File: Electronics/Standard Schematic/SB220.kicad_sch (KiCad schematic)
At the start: 134 parts, among them J1 Ant Relay, J2 ALC, J3 RF Input, J4 RF Output, J5 Screw_Terminal_01x04, J6 Screw_Terminal_01x04, J7 Screw_Terminal_01x04, K1 SB-220 Relay, M1 Fan Motor, P1 120/240 VAC 60Hz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

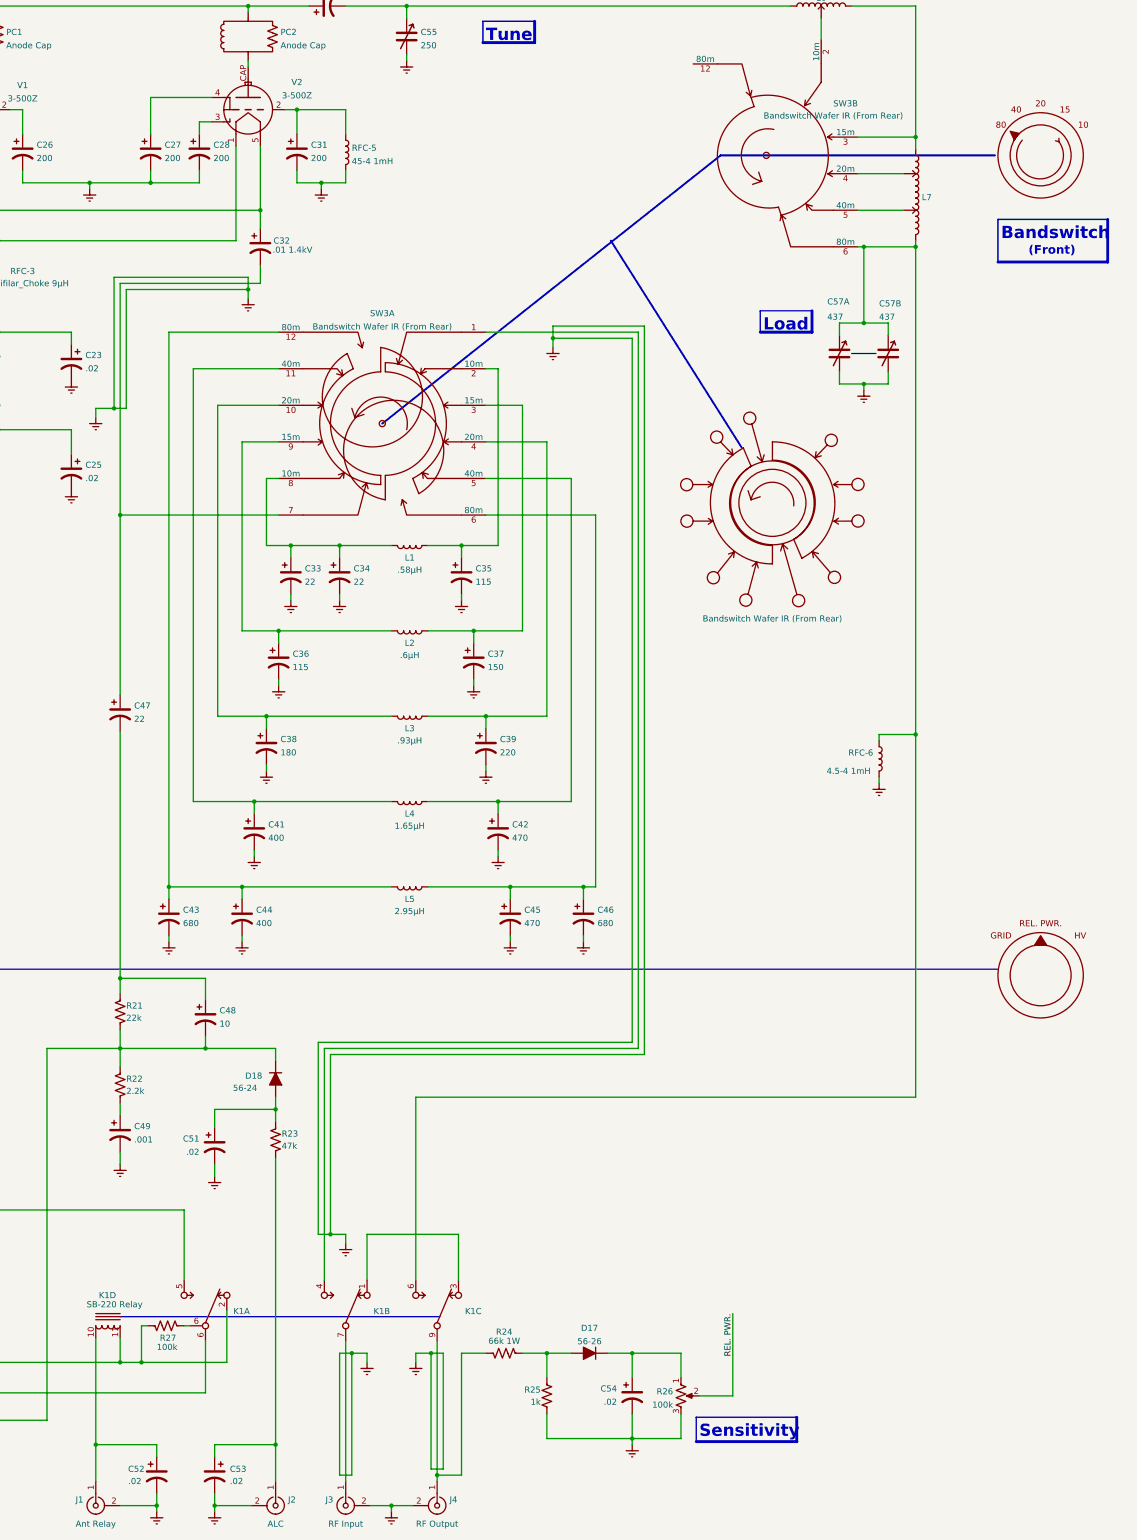
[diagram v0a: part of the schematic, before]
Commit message: Added meter switch label
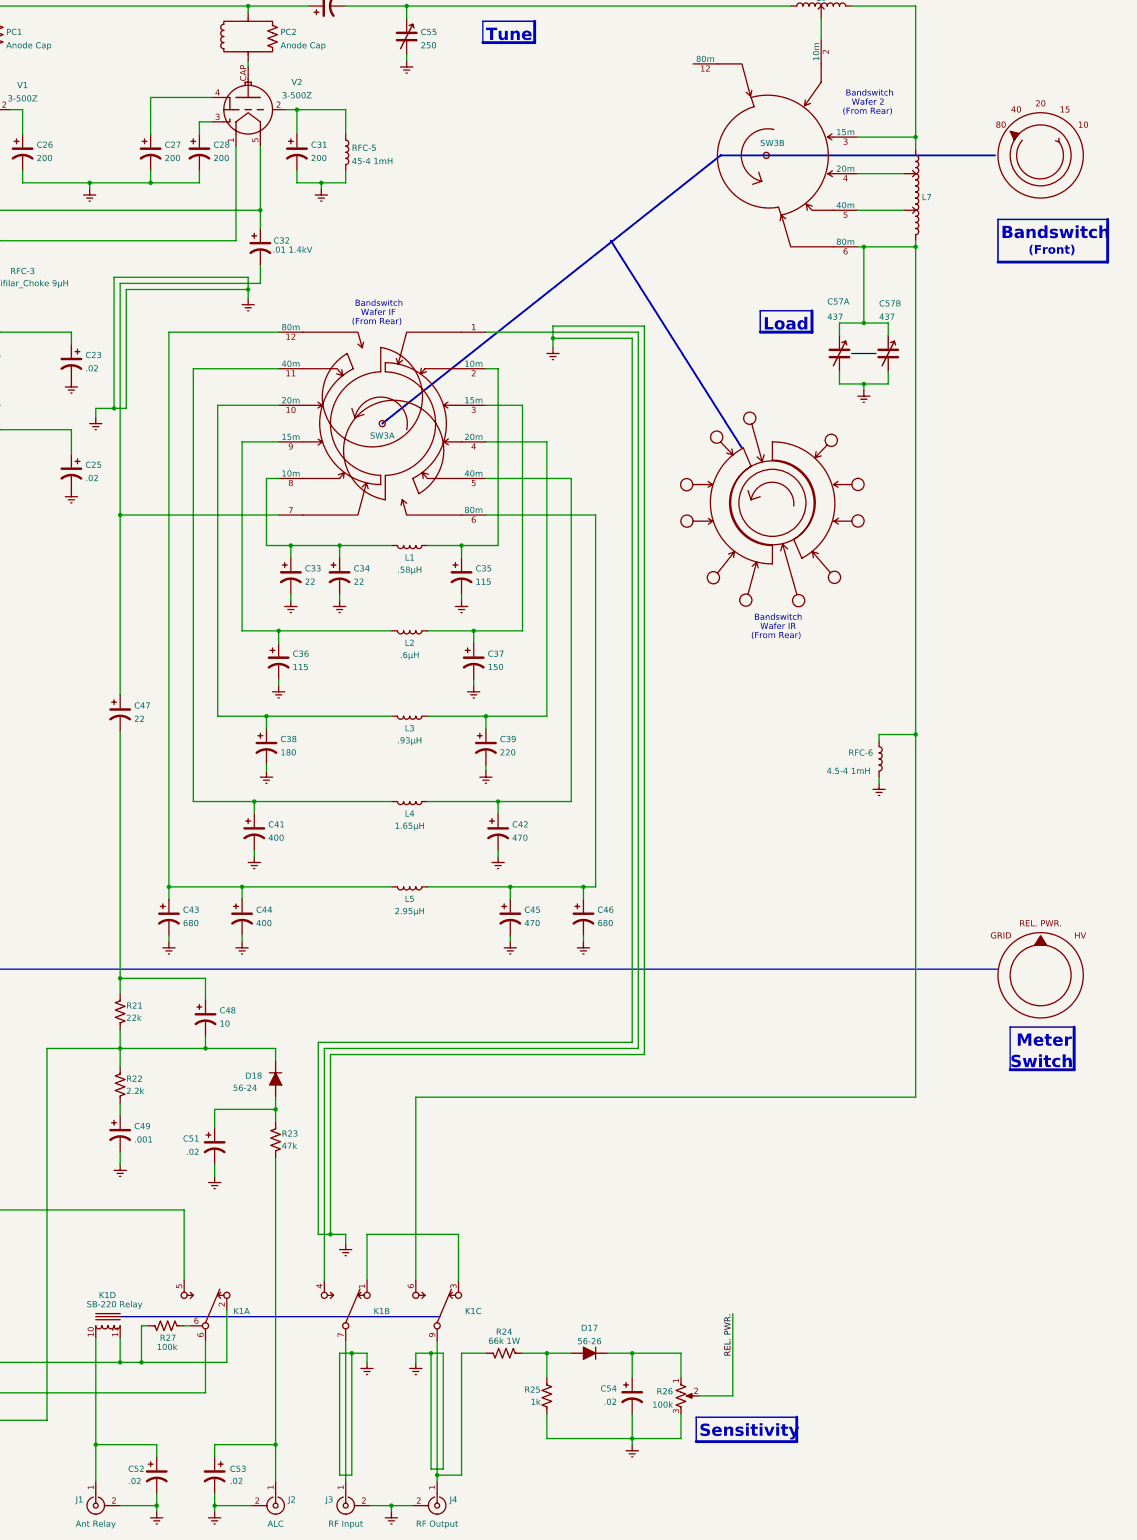
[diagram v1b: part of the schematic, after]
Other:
- note added: "(From Rear)"
- note added: "Wafer 2"
- note added: "Wafer IF"
- note added: "Wafer IR"
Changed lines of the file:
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@@
     (stroke (width 0.6) (type solid) (color 0 0 0 0))
   )
+  (polyline (pts (xy 566.42 268.605) (xy 566.42 259.715))
+    (stroke (width 0.6) (type solid) (color 0 0 0 0))
+  )
   (wire (pts (xy 177.165 287.02) (xy 295.91 287.02))
     (stroke (width 0) (type default) (color 0 0 0 0))
@@
     (stroke (width 0) (type default) (color 0 0 0 0))
   )
+  (polyline (pts (xy 553.085 259.715) (xy 553.085 268.605))
+    (stroke (width 0.3) (type solid) (color 0 0 0 0))
+  )
   (wire (pts (xy 362.585 324.485) (xy 362.585 346.71))
     (stroke (width 0) (type default) (color 0 0 0 0))
   )
+  (polyline (pts (xy 553.085 268.605) (xy 566.42 268.605))
+    (stroke (width 0.6) (type solid) (color 0 0 0 0))
+  )
   (wire (pts (xy 128.905 187.325) (xy 151.765 187.325))
     (stroke (width 0) (type default) (color 0 0 0 0))
@@
     (stroke (width 0) (type default) (color 0 0 0 0))
   )
+  (polyline (pts (xy 566.42 259.715) (xy 553.085 259.715))
+    (stroke (width 0.3) (type solid) (color 0 0 0 0))
+  )
   (wire (pts (xy 366.395 103.505) (xy 394.335 103.505))
     (stroke (width 0.3) (type dash) (color 0 0 0 0))
@@
     (effects (font (size 2.54 2.54) (thickness 0.508) bold) (justify left bottom))
   )
+  (text "Wafer IR" (at 501.015 177.165 0)
+    (effects (font (size 1.27 1.27)) (justify left bottom))
+  )
+  (text "Meter" (at 554.355 264.16 0)
+    (effects (font (size 2.54 2.54) (thickness 0.508) bold) (justify left bottom))
+  )
   (text "Strip" (at 72.39 163.83 0)
     (effects (font (size 2.54 2.54) (thickness 0.508) bold) (justify left bottom))
   )
+  (text "Wafer 2" (at 520.065 67.945 0)
+    (effects (font (size 1.27 1.27)) (justify left bottom))
+  )
   (text "Terminal" (at 69.215 160.02 0)
     (effects (font (size 2.54 2.54) (thickness 0.508) bold) (justify left bottom))
@@
     (effects (font (size 1.27 1.27)) (justify right bottom))
   )
+  (text "(From Rear)" (at 518.16 69.85 0)
+    (effects (font (size 1.27 1.27)) (justify left bottom))
+  )
   (text "Power" (at 111.76 231.775 0)
     (effects (font (size 2.54 2.54) (thickness 0.508) bold) (justify left bottom))
   )
+  (text "(From Rear)" (at 415.925 113.665 0)
+    (effects (font (size 1.27 1.27)) (justify left bottom))
+  )
+  (text "(From Rear)" (at 499.11 179.07 0)
+    (effects (font (size 1.27 1.27)) (justify left bottom))
+  )
   (text "Meter" (at 273.685 274.32 0)
     (effects (font (size 2.54 2.54) (thickness 0.508) bold) (justify left bottom))
@@
     (effects (font (size 2.54 2.54) (thickness 0.508) bold) (justify left bottom))
   )
+  (text "Bandswitch" (at 499.745 175.26 0)
+    (effects (font (size 1.27 1.27)) (justify left bottom))
+  )
   (text "Sensitivity" (at 488.315 345.44 0)
     (effects (font (size 2.54 2.54) (thickness 0.508) bold) (justify left bottom))
   )
+  (text "Bandswitch" (at 518.795 66.04 0)
+    (effects (font (size 1.27 1.27)) (justify left bottom))
+  )
   (text "(SSB Position)" (at 133.985 235.585 0)
     (effects (font (size 1.8 1.8) (thickness 0.508) bold) (justify left bottom))
   )
+  (text "Switch" (at 553.085 268.605 0)
+    (effects (font (size 2.54 2.54) (thickness 0.508) bold) (justify left bottom))
+  )
   (text "240VAC" (at 62.865 148.59 180)
     (effects (font (size 1.27 1.27)) (justify right bottom))
   )
+  (text "Wafer IF" (at 417.83 111.76 0)
+    (effects (font (size 1.27 1.27)) (justify left bottom))
+  )
   (text "(Off)" (at 114.3 238.76 0)
     (effects (font (size 1.8 1.8) (thickness 0.508) bold) (justify left bottom))
@@
     (effects (font (size 3.81 3.81)) (justify left bottom))
   )
+  (text "Bandswitch" (at 416.56 109.855 0)
+    (effects (font (size 1.27 1.27)) (justify left bottom))
+  )
   (text "Switch" (at 111.76 235.585 0)
     (effects (font (size 2.54 2.54) (thickness 0.508) bold) (justify left bottom))
@@
       (effects (font (size 1.27 1.27)) (justify left) hide)
     )
-    (property "Value" "Bandswitch Wafer IR (From Rear)" (id 1) (at 503.555 174.625 0))
+    (property "Value" "Bandswitch Wafer IR (From Rear)" (id 1) (at 503.555 174.625 0)
+      (effects (font (size 1.27 1.27)) hide)
+    )
     (property "Footprint" "" (id 2) (at 503.555 150.495 0)
       (effects (font (size 1.27 1.27)) hide)
@@
   )
   (symbol (lib_id "SB220:Bandswitch") (at 422.275 133.985 0) (unit 1)
-    (in_bom yes) (on_board yes) (fields_autoplaced)
-    (property "Reference" "SW3" (id 0) (at 422.275 111.0193 0))
-    (property "Value" "Bandswitch Wafer IR (From Rear)" (id 1) (at 422.275 113.7944 0))
+    (in_bom yes) (on_board yes)
+    (property "Reference" "SW3" (id 0) (at 422.275 136.525 0))
+    (property "Value" "Bandswitch Wafer IR (From Rear)" (id 1) (at 422.275 113.7944 0)
+      (effects (font (size 1.27 1.27)) hide)
+    )
     (property "Footprint" "" (id 2) (at 422.275 133.985 0)
       (effects (font (size 1.27 1.27)) hide)
@@
   (symbol (lib_id "SB220:Bandswitch") (at 502.285 78.105 0) (unit 2)
     (in_bom yes) (on_board yes)
-    (property "Reference" "SW3" (id 0) (at 518.795 67.31 0))
-    (property "Value" "Bandswitch Wafer IR (From Rear)" (id 1) (at 516.255 69.85 0))
+    (property "Reference" "SW3" (id 0) (at 503.555 75.565 0))
+    (property "Value" "Bandswitch Wafer IR (From Rear)" (id 1) (at 516.255 69.85 0)
+      (effects (font (size 1.27 1.27)) hide)
+    )
     (property "Footprint" "" (id 2) (at 502.285 78.105 0)
       (effects (font (size 1.27 1.27)) hide)
